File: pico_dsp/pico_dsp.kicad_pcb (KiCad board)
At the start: 2 copper layers, 81 parts, among them J1 HDR_20, J2 HDR_20, J3 SJ3-35082B-TR, J4 SJ3-35082B-TR, J5 SJ3-35082B-TR, J7 SJ3-35082B-TR, SW1 RotaryEncoder_Switch, SW2 RotaryEncoder_Switch, U1 PCM5102A, U2 PCM1802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

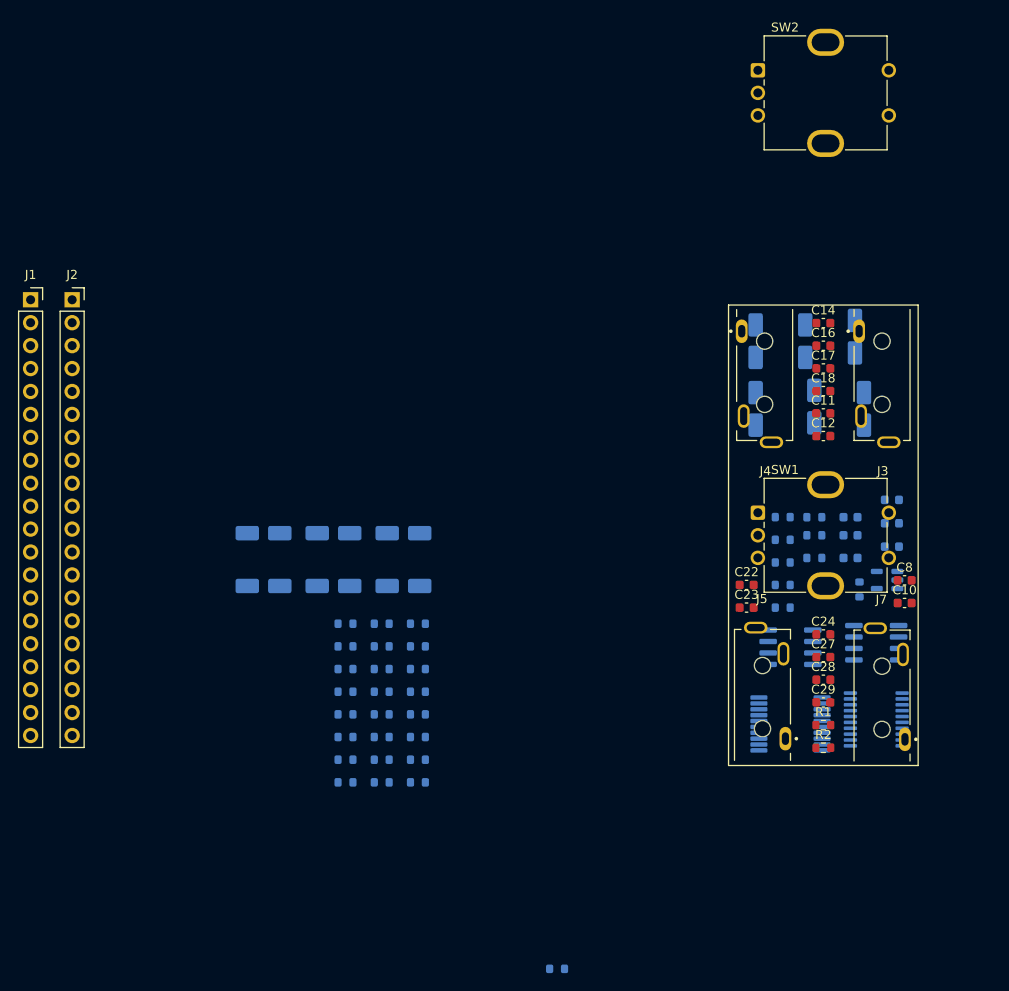
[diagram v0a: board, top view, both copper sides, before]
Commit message: Added pads and updated pcb
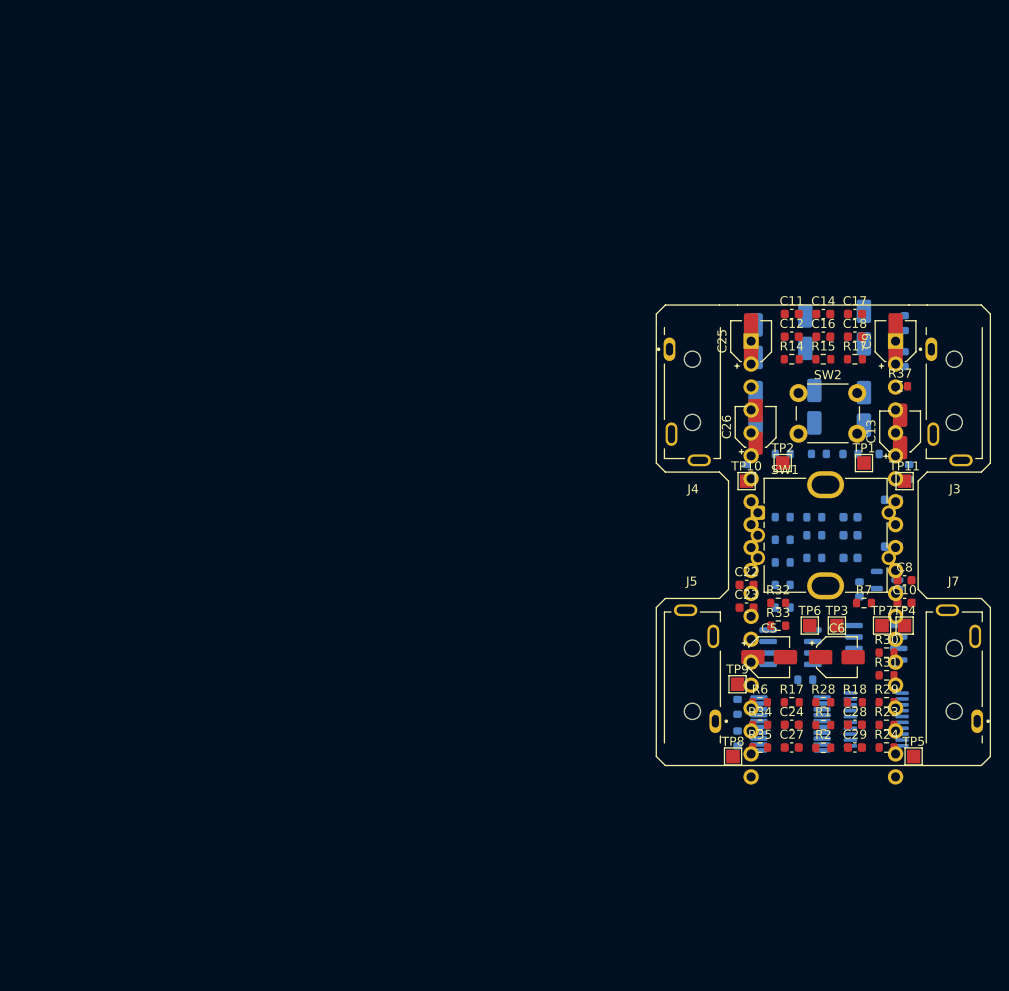
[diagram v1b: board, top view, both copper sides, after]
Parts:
- removed D2: LED_Green, LED_SMD:LED_0603_1608Metric
- added R14: 0R, Resistor_SMD:R_0603_1608Metric, F.Cu at (201.5, 83.0)
- added R15: 0R, Resistor_SMD:R_0603_1608Metric, F.Cu at (205.0, 83.0)
- added R17: 0R, Resistor_SMD:R_0603_1608Metric, F.Cu at (208.5, 83.0)
- added R37: 0R, Resistor_SMD:R_0603_1608Metric, F.Cu at (213.5, 86.0)
- added TP1: TestPoint, TestPoint:TestPoint_Pad_1.5x1.5mm, F.Cu at (209.5, 94.5)
- added TP10: TestPoint, TestPoint:TestPoint_Pad_1.5x1.5mm, F.Cu at (196.5, 96.5)
- added TP11: TestPoint, TestPoint:TestPoint_Pad_1.5x1.5mm, F.Cu at (214.0, 96.5)
- added TP2: TestPoint, TestPoint:TestPoint_Pad_1.5x1.5mm, F.Cu at (200.5, 94.5)
- added TP3: TestPoint, TestPoint:TestPoint_Pad_1.5x1.5mm, F.Cu at (206.5, 112.5)
- added TP4: TestPoint, TestPoint:TestPoint_Pad_1.5x1.5mm, F.Cu at (214.0, 112.5)
- added TP5: TestPoint, TestPoint:TestPoint_Pad_1.5x1.5mm, F.Cu at (215.0, 127.0)
- added TP6: TestPoint, TestPoint:TestPoint_Pad_1.5x1.5mm, F.Cu at (203.5, 112.5)
- added TP7: TestPoint, TestPoint:TestPoint_Pad_1.5x1.5mm, F.Cu at (211.5, 112.5)
- added TP8: TestPoint, TestPoint:TestPoint_Pad_1.5x1.5mm, F.Cu at (195.0, 127.0)
- added TP9: TestPoint, TestPoint:TestPoint_Pad_1.5x1.5mm, F.Cu at (195.5, 119.0)
- C13, C25, C26, C5, C6, C9, R18, R23, R24, R28, R29, R30, R31, R32, R33, R34, R35, R6, R7: moved to F.Cu
- J1, J2: moved to B.Cu
- J3, J4, J5, J7: footprint SJ3-35082B-TR:SAMESKY_SJ3-35082B-TR -> Kicad-symbols:SAMESKY_SJ3-35082B-TR
- R14, R15: value 10k -> 0R
- R17: value 120R -> 0R; moved to F.Cu
- SW2: value RotaryEncoder_Switch -> SW_Push; footprint Rotary_Encoder:RotaryEncoder_Bourns_Vertical_PEC12R-3x17F-Sxxxx -> Button_Switch_THT:SW_PUSH_6mm
- moved J1 95.9 mm to (213.0, 81.0), turned to 180 degrees
- moved J2 75.3 mm to (197.0, 81.0), turned to 180 degrees
- moved R21 72.3 mm to (214.0, 79.0), turned to -90 degrees
- moved R22 71.4 mm to (214.0, 83.0), turned to -90 degrees
- moved C9 65.8 mm to (213.0, 81.0), turned to 90 degrees
- moved C13 65.0 mm to (213.5, 91.0), turned to 90 degrees
- moved R11 61.8 mm to (214.5, 95.5), turned to -90 degrees
- moved R29 60.2 mm to (212.0, 121.0), turned to 0 degrees
- moved R30 60.0 mm to (212.0, 115.5), turned to 0 degrees
- moved R31 60.0 mm to (212.0, 118.0), turned to 0 degrees
- moved R20 58.2 mm to (208.0, 93.5)
- moved R9 58.2 mm to (212.0, 93.5)
- moved C25 58.0 mm to (197.0, 81.0), turned to 90 degrees
- moved C26 57.3 mm to (197.5, 90.5), turned to 90 degrees
- moved R23 56.0 mm to (212.0, 123.5), turned to 0 degrees
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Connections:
- C17 pad 1: /OutL -> /OutL_DAC
- C18 pad 1: /OutR -> /OutR_DAC
- D3 pad 1: /Led_3 -> /Led_2
- J1 pad 20: /Enc2_SW -> unconnected-(J1-Pin_20-Pad20)
- J2 pad 21: /Led_3 -> unconnected-(J2-Pin_20-Pad21)
- J2 pad 29: /Enc2_DT -> unconnected-(J2-Pin_29-Pad29)
- J2 pad 30: unconnected-(J2-Pin_30-Pad30) -> Net-(J2-Pin_30)
- J2 pad 31: /Enc2_CLK -> unconnected-(J2-Pin_31-Pad31)
- J3 pad 2: Net-(J3-Pad2) -> /InR_Jack
- J7 pad 2: Net-(J7-Pad2) -> /InL_Jack
- R10 pad 1: /OutL -> /OutL_DAC
- R11 pad 1: /OutR -> /OutR_DAC
- R14 pad 1: +3.3V -> /InL_Jack
- R14 pad 2: /Enc2_DT -> /ADC_L
- R15 pad 1: +3.3V -> /InR_Jack
- R15 pad 2: /Enc2_CLK -> /ADC_R
- R17 pad 1: Net-(D2-A) -> /OutL_DAC
- R17 pad 2: +3.3V -> /OutL
- R18 pad 1: Net-(J7-Pad2) -> /ADC_L
- R20 pad 1: Net-(J3-Pad2) -> /ADC_R
